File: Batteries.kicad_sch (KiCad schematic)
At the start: 24 parts

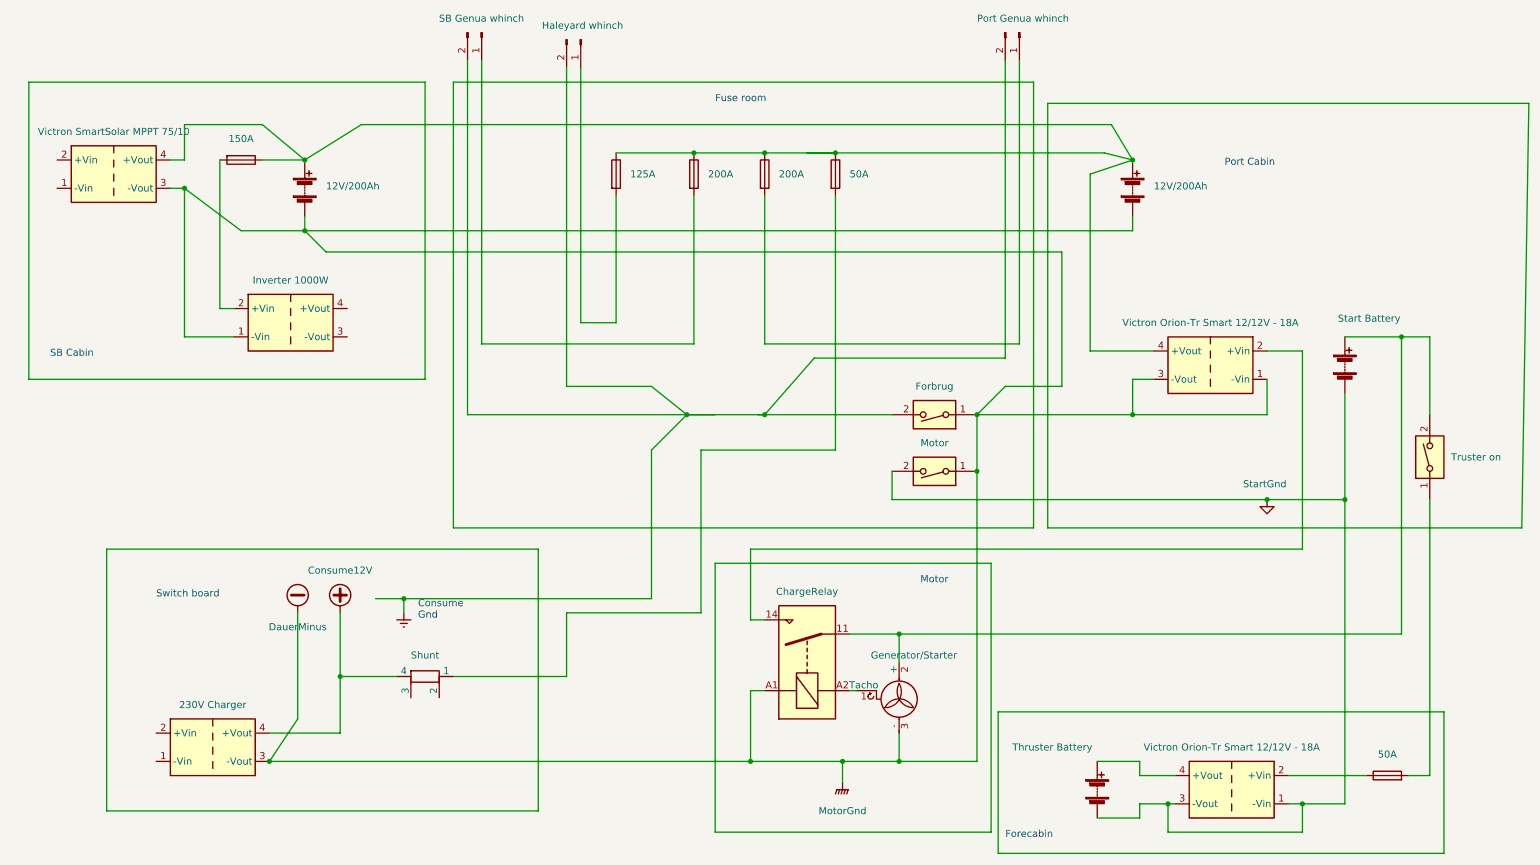
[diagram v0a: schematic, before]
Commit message: An older version more likely to work
In this circuit house bank will charge the Thuster
battery.
Originally - when tried - the Thruster DC/DC
swictch -on threshold was set far too high, meaning
it would never be reached if voltage on house bank
was low.
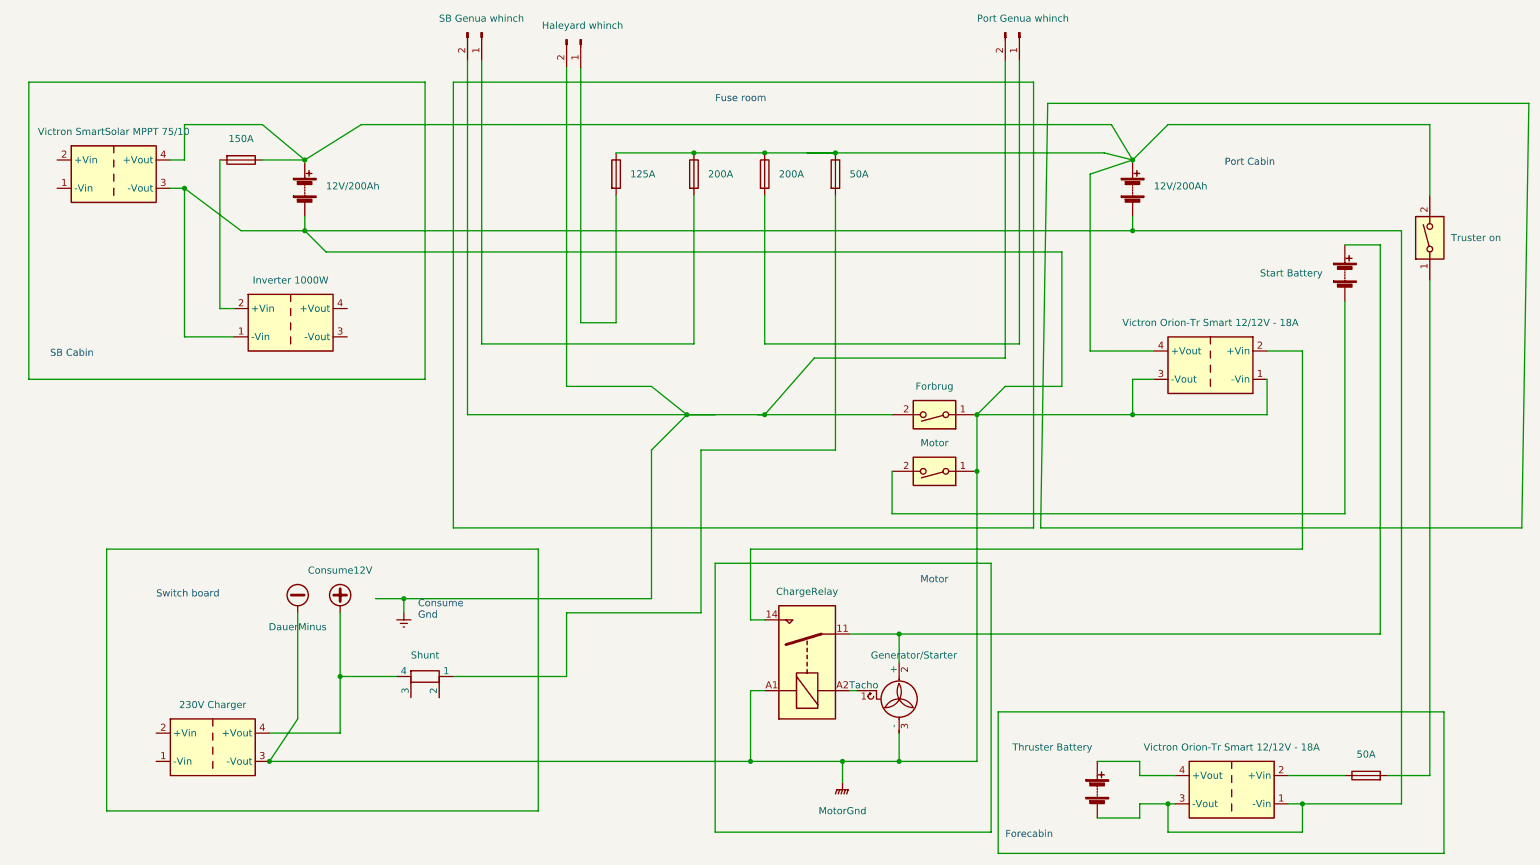
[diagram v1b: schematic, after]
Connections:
- net -VDC: now also BT?.2 (-), PS?.1 (-Vin), PS?.3 (-Vout)
- net at BT?.1 (+), BT?.1 (+), F?.1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: now also SW?.2
- net at BT?.1 (+), ChargeRelay.11, Generator/Starter.2 (+): no longer SW?.2
- removed net StartGnd: BT?.2 (-), BT?.2 (-), PS?.1 (-Vin), PS?.3 (-Vout), SW?.2
- new net: BT?.2 (-), SW?.2

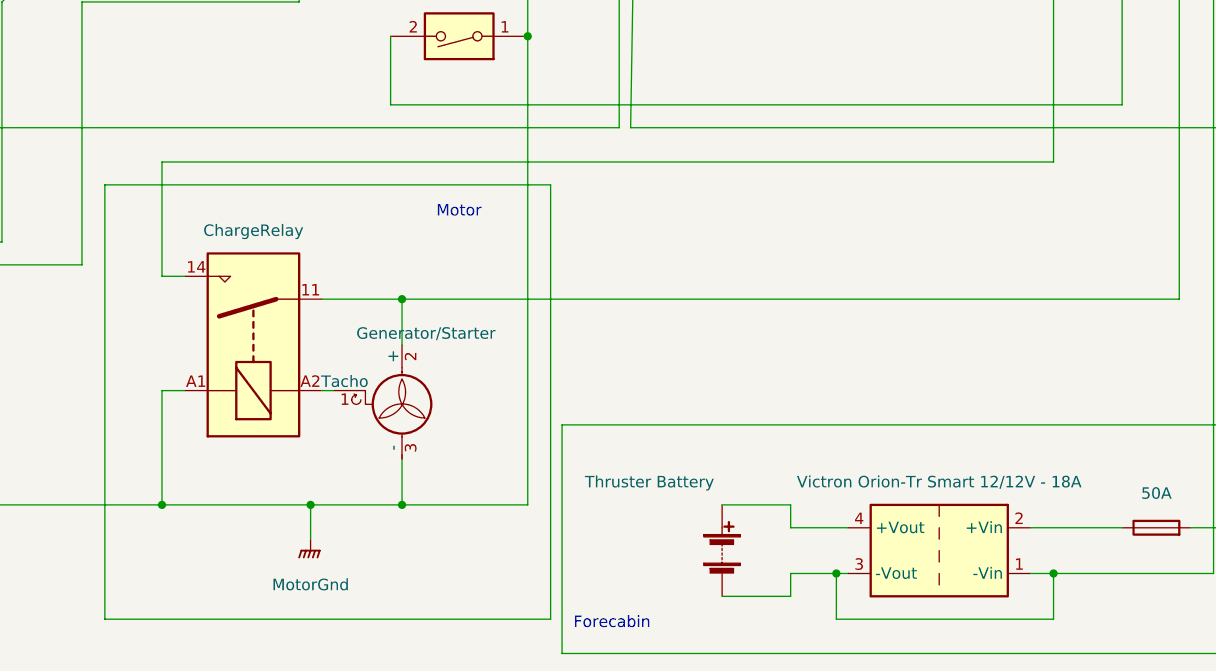
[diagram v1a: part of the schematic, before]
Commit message: v2506: Old charge relay bypassed.
README file added.
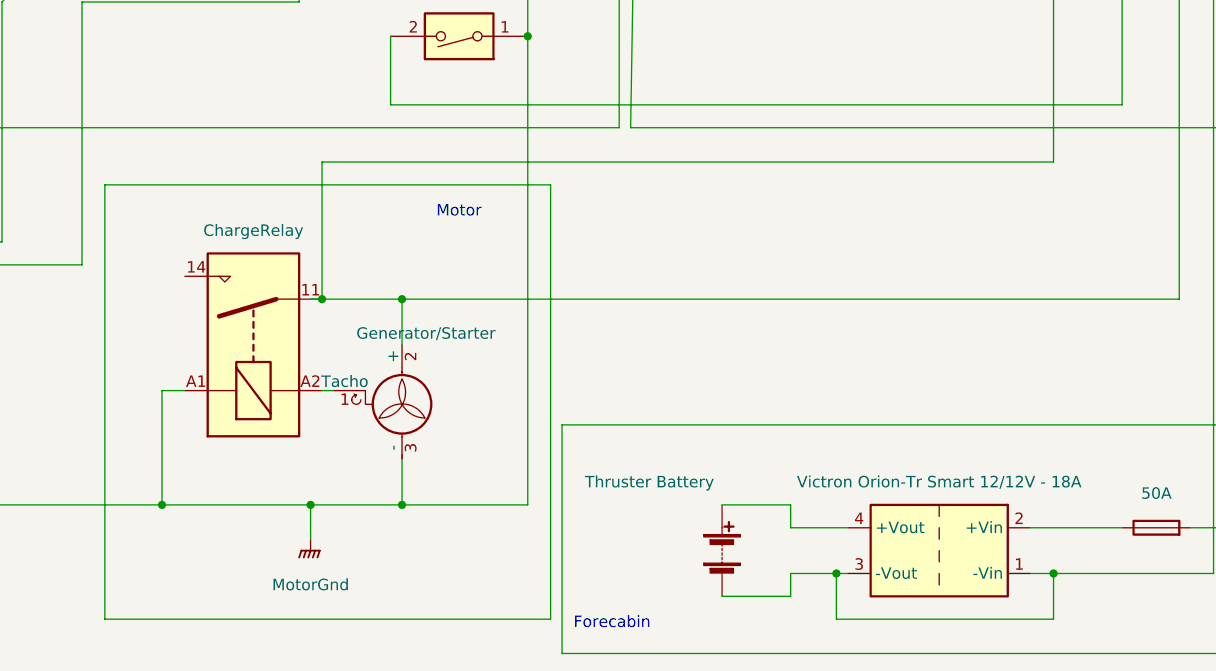
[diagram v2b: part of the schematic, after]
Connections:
- net at BT?.1 (+), ChargeRelay.11, Generator/Starter.2 (+): now also PS?.2 (+Vin)
- net at ChargeRelay.14: no longer PS?.2 (+Vin)

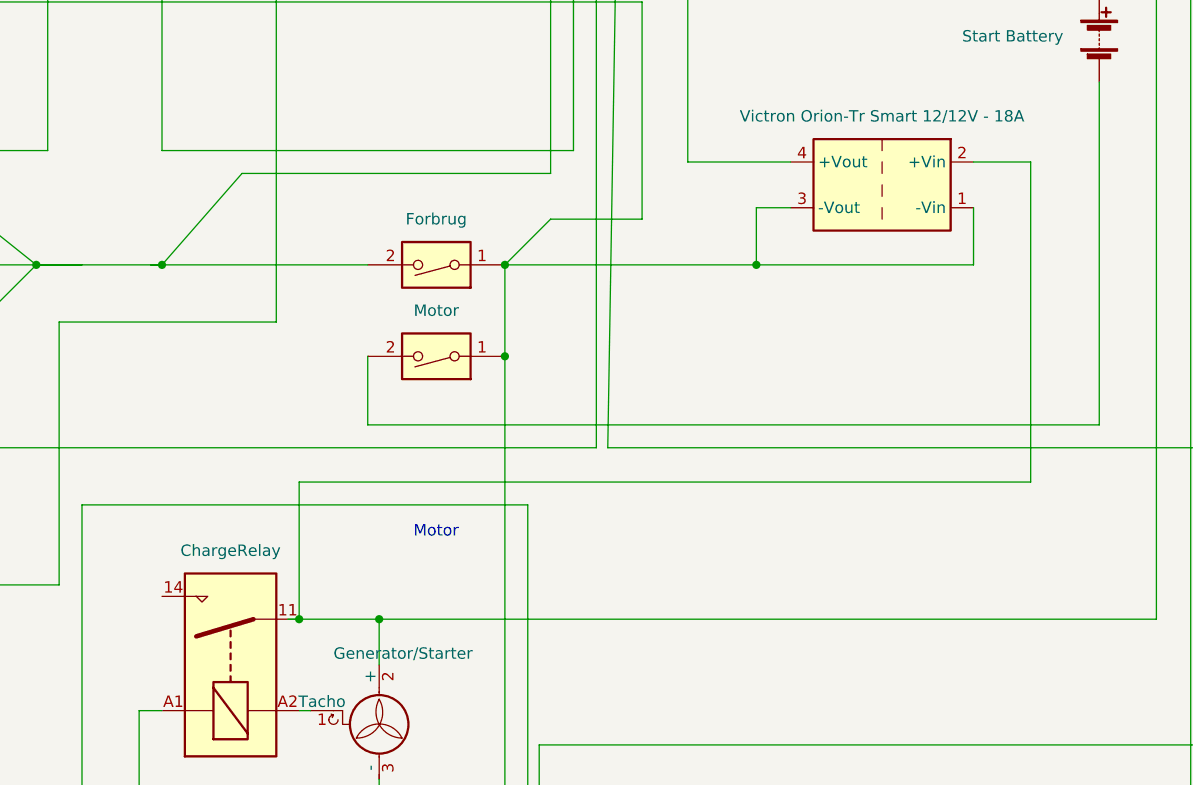
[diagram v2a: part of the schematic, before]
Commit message: Input to house-bank DC-DC moved to output of chargerelay. If the chargerelay is bypassed, starter battery will constantly provide power to house-bank DC-DC. Even though it is spec'ed to be below 80mA a little battery as the starter will during the winter be discharged. Furthermore the thought of not being fully assured about start battery state isn't good
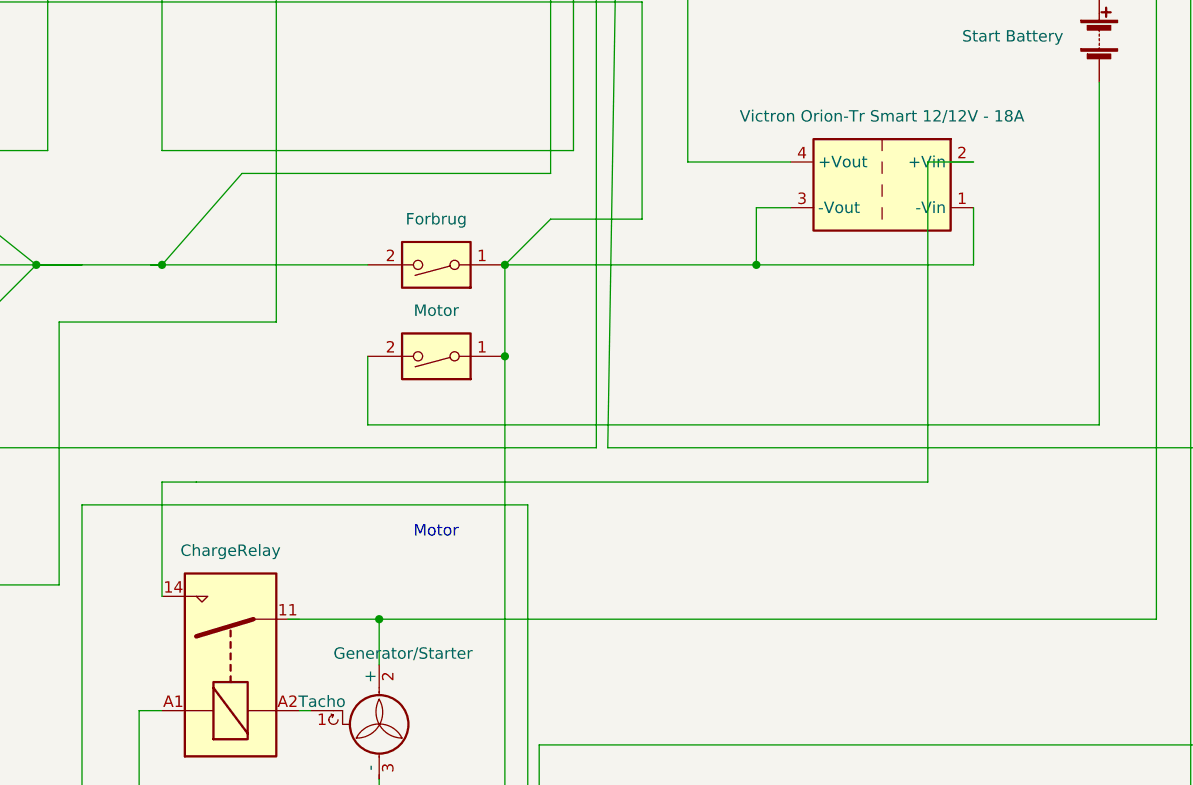
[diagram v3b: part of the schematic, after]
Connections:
- net at BT?.1 (+), Generator/Starter.2 (+): no longer ChargeRelay.11, PS?.2 (+Vin)
- net at ChargeRelay.14: now also PS?.2 (+Vin)
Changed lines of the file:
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@@
-	)
-	(junction
-		(at 160.02 125.73)
-		(diameter 0)
-		(color 0 0 0 0)
 	)
 	(junction
@@
 	(wire
 		(pts
+			(xy 144.78 110.49) (xy 148.59 110.49)
+		)
+		(stroke
+			(width 0)
+			(type dot)
+			(color 255 0 0 1)
+		)
+	)
+	(wire
+		(pts
 			(xy 264.16 34.29) (xy 264.16 46.99)
 		)
@@
 	(wire
 		(pts
-			(xy 168.91 125.73) (xy 160.02 125.73)
+			(xy 158.75 125.73) (xy 168.91 125.73)
 		)
 		(stroke
@@
 	(wire
 		(pts
-			(xy 241.3 110.49) (xy 241.3 74.93)
+			(xy 229.87 110.49) (xy 229.87 74.93)
 		)
 		(stroke
@@
 	(wire
 		(pts
+			(xy 144.78 123.19) (xy 144.78 110.49)
+		)
+		(stroke
+			(width 0)
+			(type dot)
+			(color 255 0 0 1)
+		)
+	)
+	(wire
+		(pts
 			(xy 38.1 40.64) (xy 40.64 40.64)
 		)
@@
 	(wire
 		(pts
-			(xy 158.75 125.73) (xy 160.02 125.73)
-		)
-		(stroke
-			(width 0)
-			(type default)
-		)
-	)
-	(wire
-		(pts
-			(xy 241.3 74.93) (xy 234.95 74.93)
-		)
-		(stroke
-			(width 0)
-			(type dot)
-			(color 255 0 0 1)
-		)
-	)
-	(wire
-		(pts
-			(xy 160.02 110.49) (xy 160.02 125.73)
+			(xy 229.87 74.93) (xy 234.95 74.93)
 		)
 		(stroke
@@
 	(wire
 		(pts
-			(xy 160.02 110.49) (xy 241.3 110.49)
-		)
-		(stroke
+			(xy 148.59 110.49) (xy 229.87 110.49)
+		)
+		(stroke
